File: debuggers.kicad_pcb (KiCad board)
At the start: 2 copper layers, 7 parts, among them P1 TI_JTAG, P2 SWD, P3 TI_jtag, P4 SWD+SWO+UART

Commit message: Updated files for production
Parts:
- 5v1: value Jumper_NO_Small -> PWR
- moved 5v1 50.4 mm to (136.0, 67.9)
- moved P4 50.4 mm to (139.8, 90.7)
- moved P2 50.4 mm to (130.9, 92.0)
- moved R2 43.5 mm to (111.3, 90.8)
- moved P1 43.5 mm to (108.7, 69.2)
- moved R1 43.5 mm to (107.5, 90.8)
- moved P3 40.6 mm to (120.7, 69.4)
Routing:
- net /TI_GND: track 31.5 -> 0.00 mm
- net /GND_ARM: track 44.0 -> 26.2 mm
- net /JLINK_TX: track 31.5 -> 16.6 mm
- net /Trst: track 19.9 -> 10.6 mm
- net /3v3: track 56.6 -> 50.3 mm
- net /VTref: track 40.7 -> 34.7 mm
- net /TCK: track 13.8 -> 13.1 mm
- net /TDO: track 13.8 -> 13.2 mm
- added copper zone on B.Cu, net /GND_ARM
- added copper zone on F.Cu, net /GND_ARM
- added copper zone on B.Cu, net /TI_GND
- added copper zone on F.Cu, net /TI_GND
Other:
- board outline added: 39 x 32 mm
- rule trace_min: 0.2 -> 0.1524
- rule via_min_size: 0.4 -> 0.1524

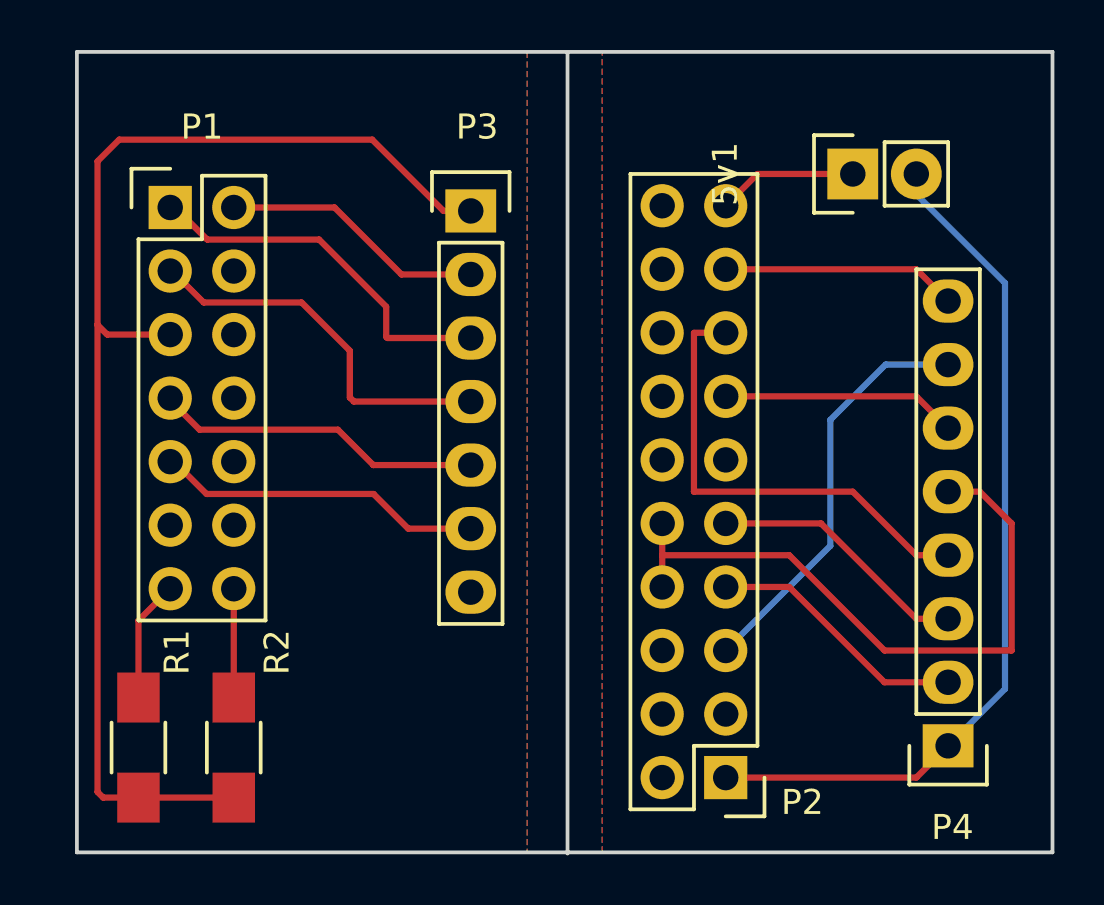
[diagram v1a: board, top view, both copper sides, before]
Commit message: Created Seperate boards for each debugger
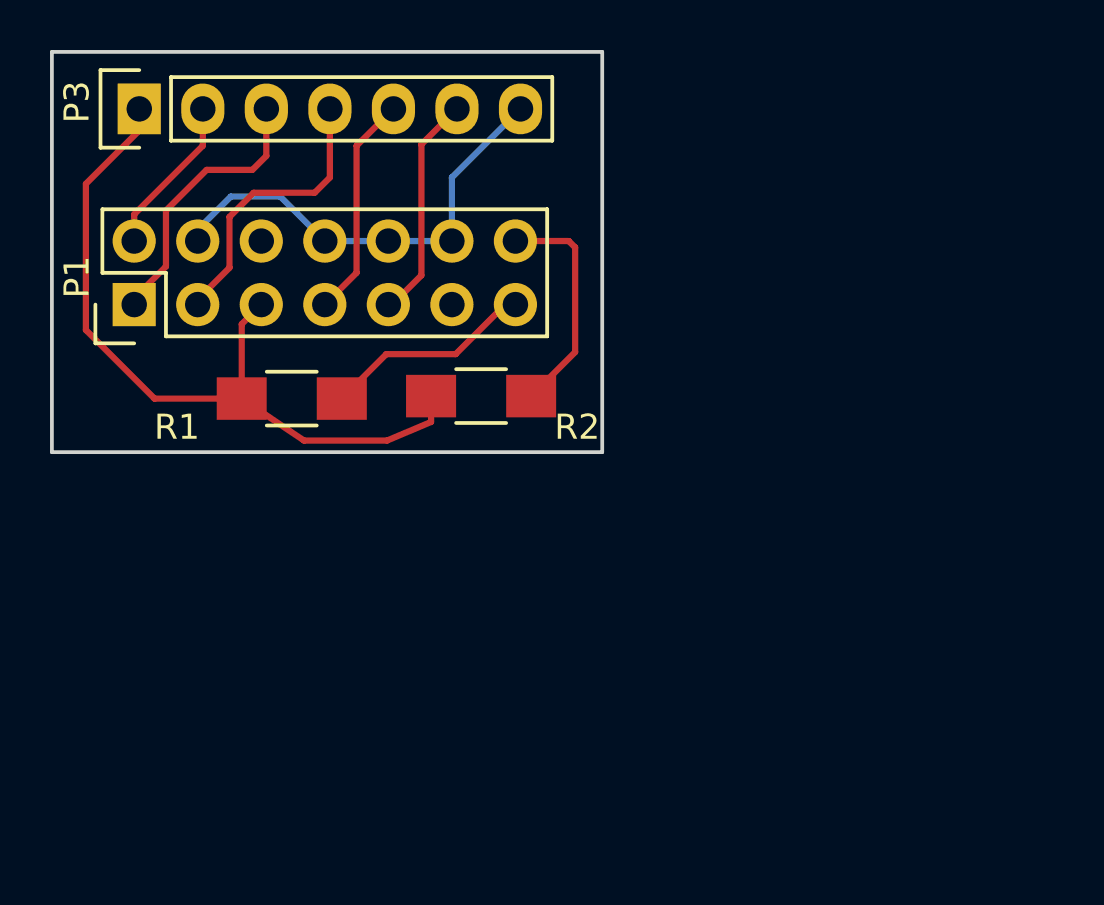
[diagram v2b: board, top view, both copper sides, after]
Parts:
- removed 5v1: PWR, Pin_Headers:Pin_Header_Straight_1x02
- removed P2: SWD, Pin_Headers:Pin_Header_Straight_2x10
- removed P4: SWD+SWO+UART, Pin_Headers:Pin_Header_Straight_1x08
- moved R2 17.2 mm to (121.2, 76.8), turned to 180 degrees
- moved R1 15.2 mm to (113.6, 76.9), turned to 180 degrees
- moved P3 13.9 mm to (107.5, 65.3), turned to 90 degrees
- moved P1 4.14 mm to (107.3, 73.1), turned to 90 degrees
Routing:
- net /VTref: track 34.7 -> 0.00 mm
- net /GND_ARM: track 26.2 -> 0.00 mm
- net /3v3: track 50.3 -> 30.4 mm
- net /RESET: track 18.8 -> 0.00 mm
- net /TI_GND: track 0.00 -> 18.3 mm
- net /JLINK_TX: track 16.6 -> 0.00 mm
- net /SWDIO: track 10.5 -> 0.00 mm
- net /SWDCLK: track 10.5 -> 0.00 mm
- net /JLINK_RX: track 9.42 -> 0.00 mm
- net /SWO: track 9.42 -> 0.00 mm
- net /5v_Supply: track 5.61 -> 0.00 mm
- net Net-(P1-Pad14): track 4.35 -> 9.17 mm
- net /TDO: track 13.2 -> 8.96 mm
- net /Trst: track 10.6 -> 6.42 mm
- net /TCK: track 13.1 -> 9.05 mm
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- removed copper zone on B.Cu, net /GND_ARM
- removed copper zone on F.Cu, net /GND_ARM
- removed copper zone on B.Cu, net /TI_GND
- removed copper zone on F.Cu, net /TI_GND
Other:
- board size 39 x 32 mm -> 22 x 16 mm
